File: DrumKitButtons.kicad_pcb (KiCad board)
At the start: 2 copper layers, 124.5 x 40.2 mm, 25 parts, among them J1 Input, J2 Output, U1 74HC165, U2 TLC5916

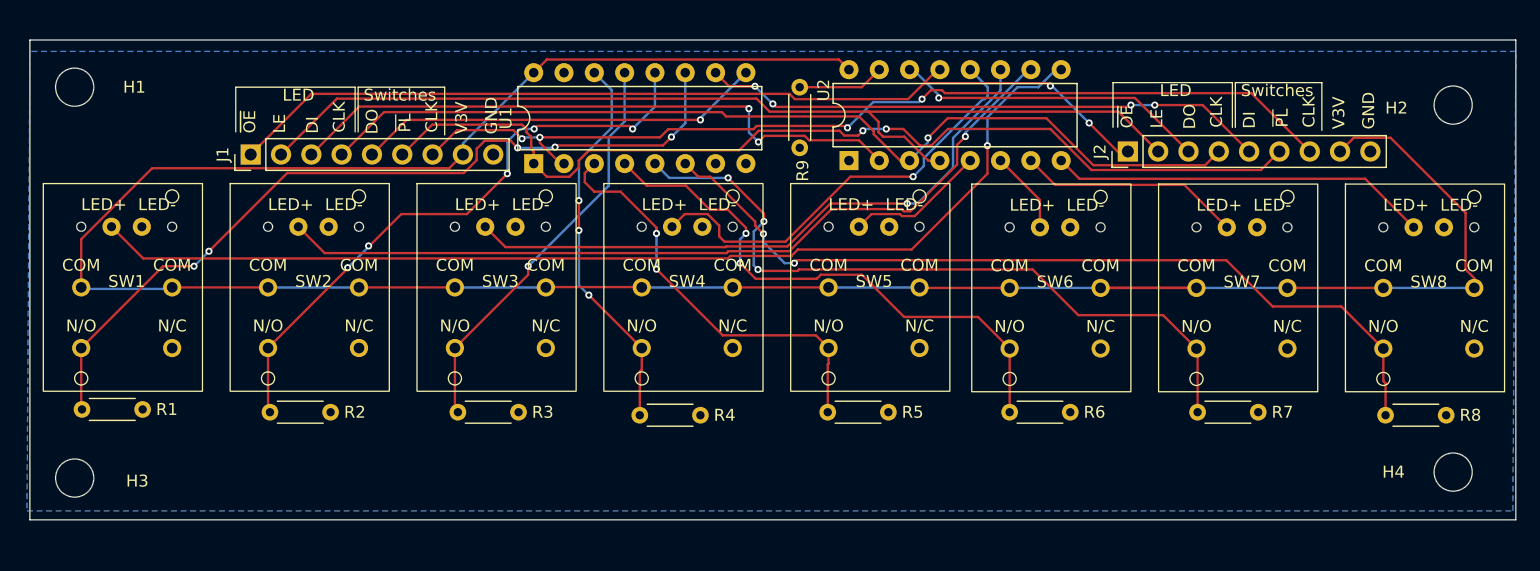
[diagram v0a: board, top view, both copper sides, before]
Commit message: Move 74HC165 to bottom
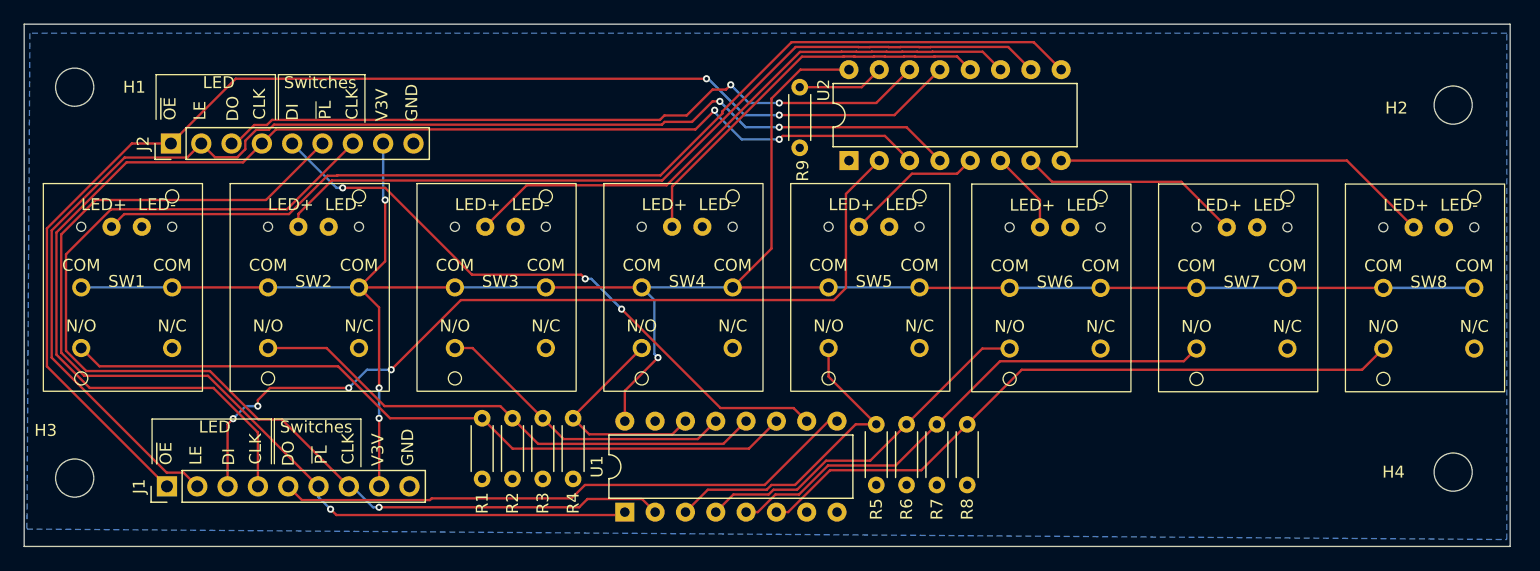
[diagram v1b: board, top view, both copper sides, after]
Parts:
- moved J2 80.2 mm to (62.3, 55.7)
- moved R8 35.1 mm to (129.0, 79.2), turned to -90 degrees
- moved R1 33.5 mm to (88.4, 78.7), turned to -90 degrees
- moved U1 30.2 mm to (100.3, 86.6)
- moved J1 28.7 mm to (62.0, 84.4)
- moved R7 21.9 mm to (126.5, 79.2), turned to -90 degrees
- moved R2 20.3 mm to (90.9, 78.7), turned to -90 degrees
- moved R6 8.70 mm to (124.0, 79.2), turned to -90 degrees
- moved R3 7.13 mm to (93.5, 78.7), turned to -90 degrees
- moved R4 5.59 mm to (96.0, 78.7), turned to -90 degrees
- moved R5 4.19 mm to (121.4, 79.2), turned to -90 degrees
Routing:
- net /DO_{LED}: track 26.0 -> 60.6 mm, vias 1 -> 2
- net VCC: track 219.7 -> 185.2 mm, vias 0 -> 4
- net /CLK_{LED}: track 80.6 -> 112.1 mm, vias 1 -> 2
- net /~{OE_{LED}}: track 80.3 -> 108.6 mm
- net /LE_{LED}: track 85.5 -> 110.1 mm, vias 0 -> 2
- net /DI_{LED}: track 52.7 -> 73.9 mm, vias 2 -> 4
- net /SW_{7}: track 61.0 -> 43.4 mm, vias 3 -> 0
- net /SW_{6}: track 46.7 -> 30.3 mm, vias 2 -> 0
- net /DO_{SW}: track 34.3 -> 49.2 mm, vias 1 -> 0
- net /SW_{8}: track 71.4 -> 56.5 mm, vias 2 -> 0
- net /SW_{4}: track 32.7 -> 18.7 mm, vias 3 -> 0
- net /CLK_{SW}: track 81.8 -> 91.5 mm, vias 4 -> 1
- net /SW_{3}: track 34.4 -> 25.6 mm, vias 1 -> 0
- net /SW_{5}: track 35.5 -> 27.1 mm, vias 2 -> 0
- net /SW_{2}: track 50.9 -> 44.2 mm, vias 5 -> 0
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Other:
- board size 124.5 x 40.2 mm -> 124.5 x 43.8 mm
